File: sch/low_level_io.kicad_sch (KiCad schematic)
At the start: 10 parts, among them J401 Extension, SW401 RESET_Sw, SW402 USER_Sw

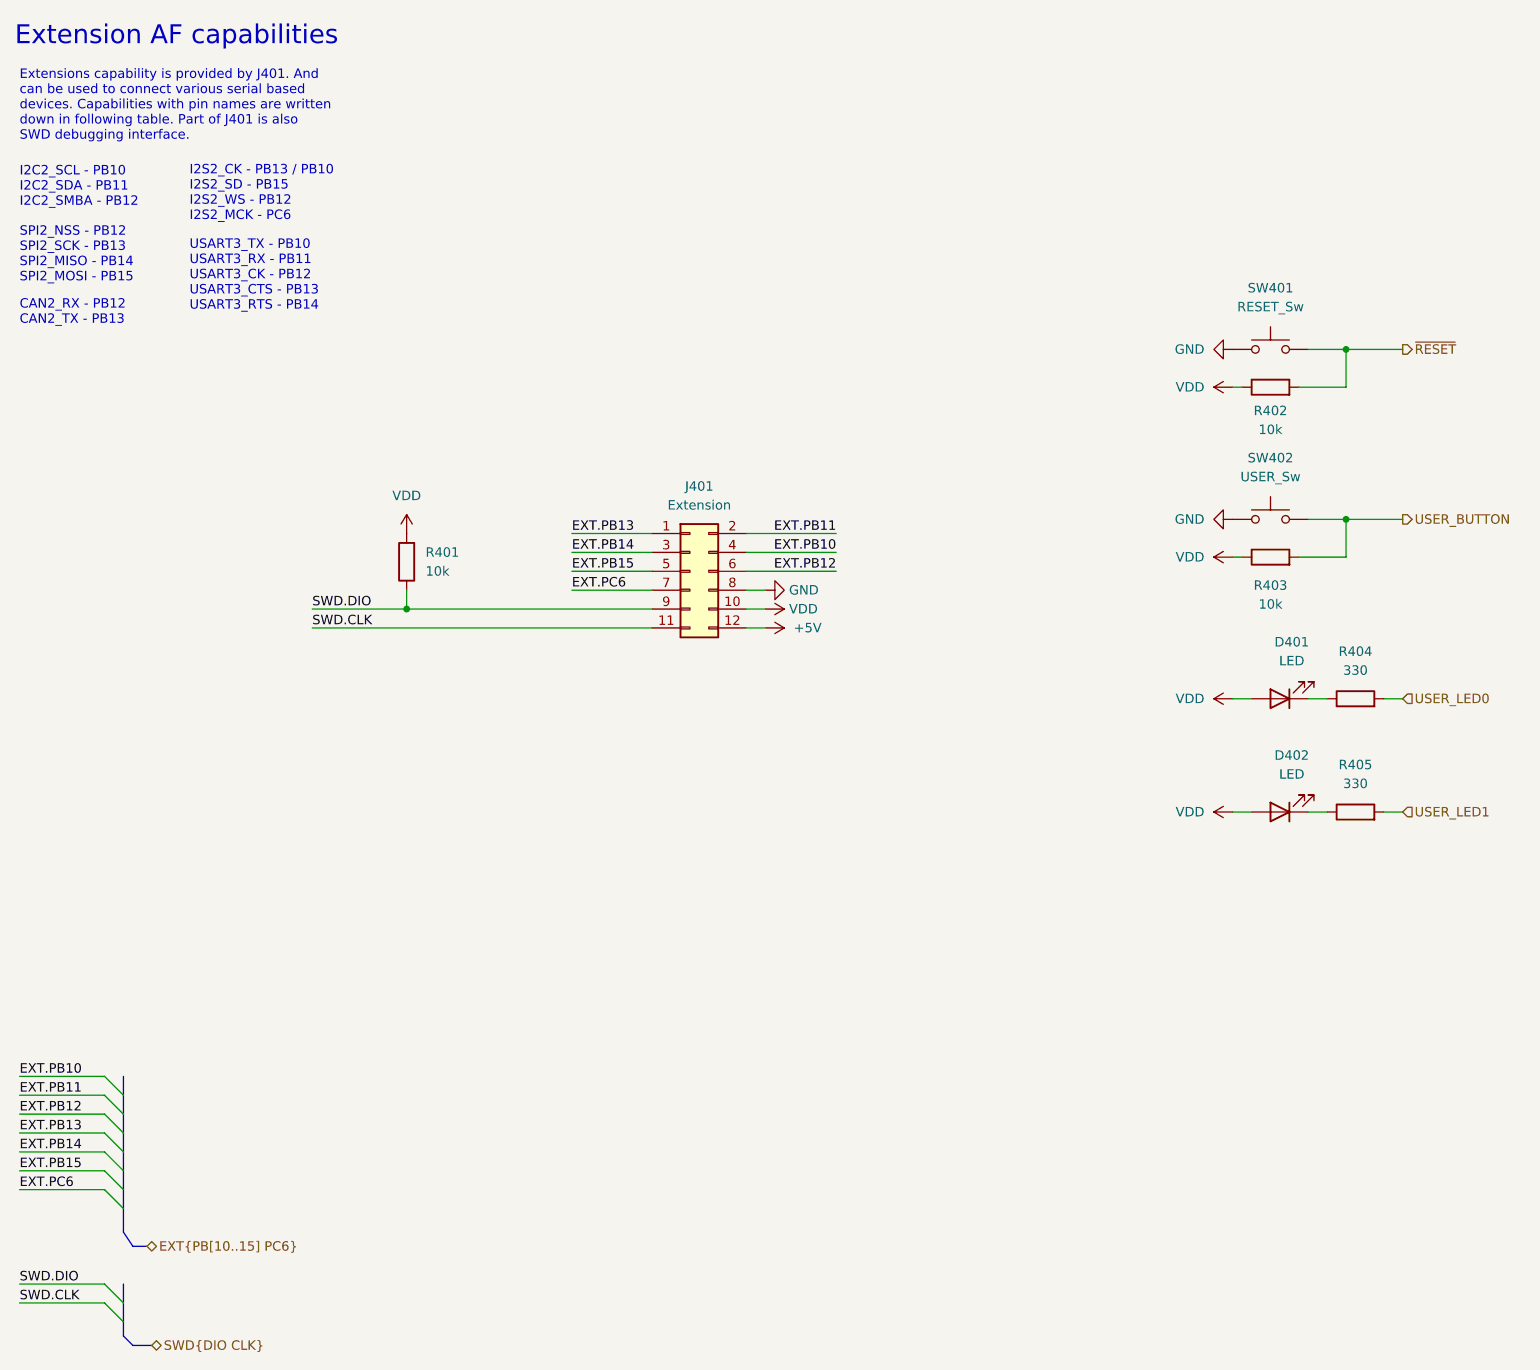
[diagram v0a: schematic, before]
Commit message: Added more expansion capability.
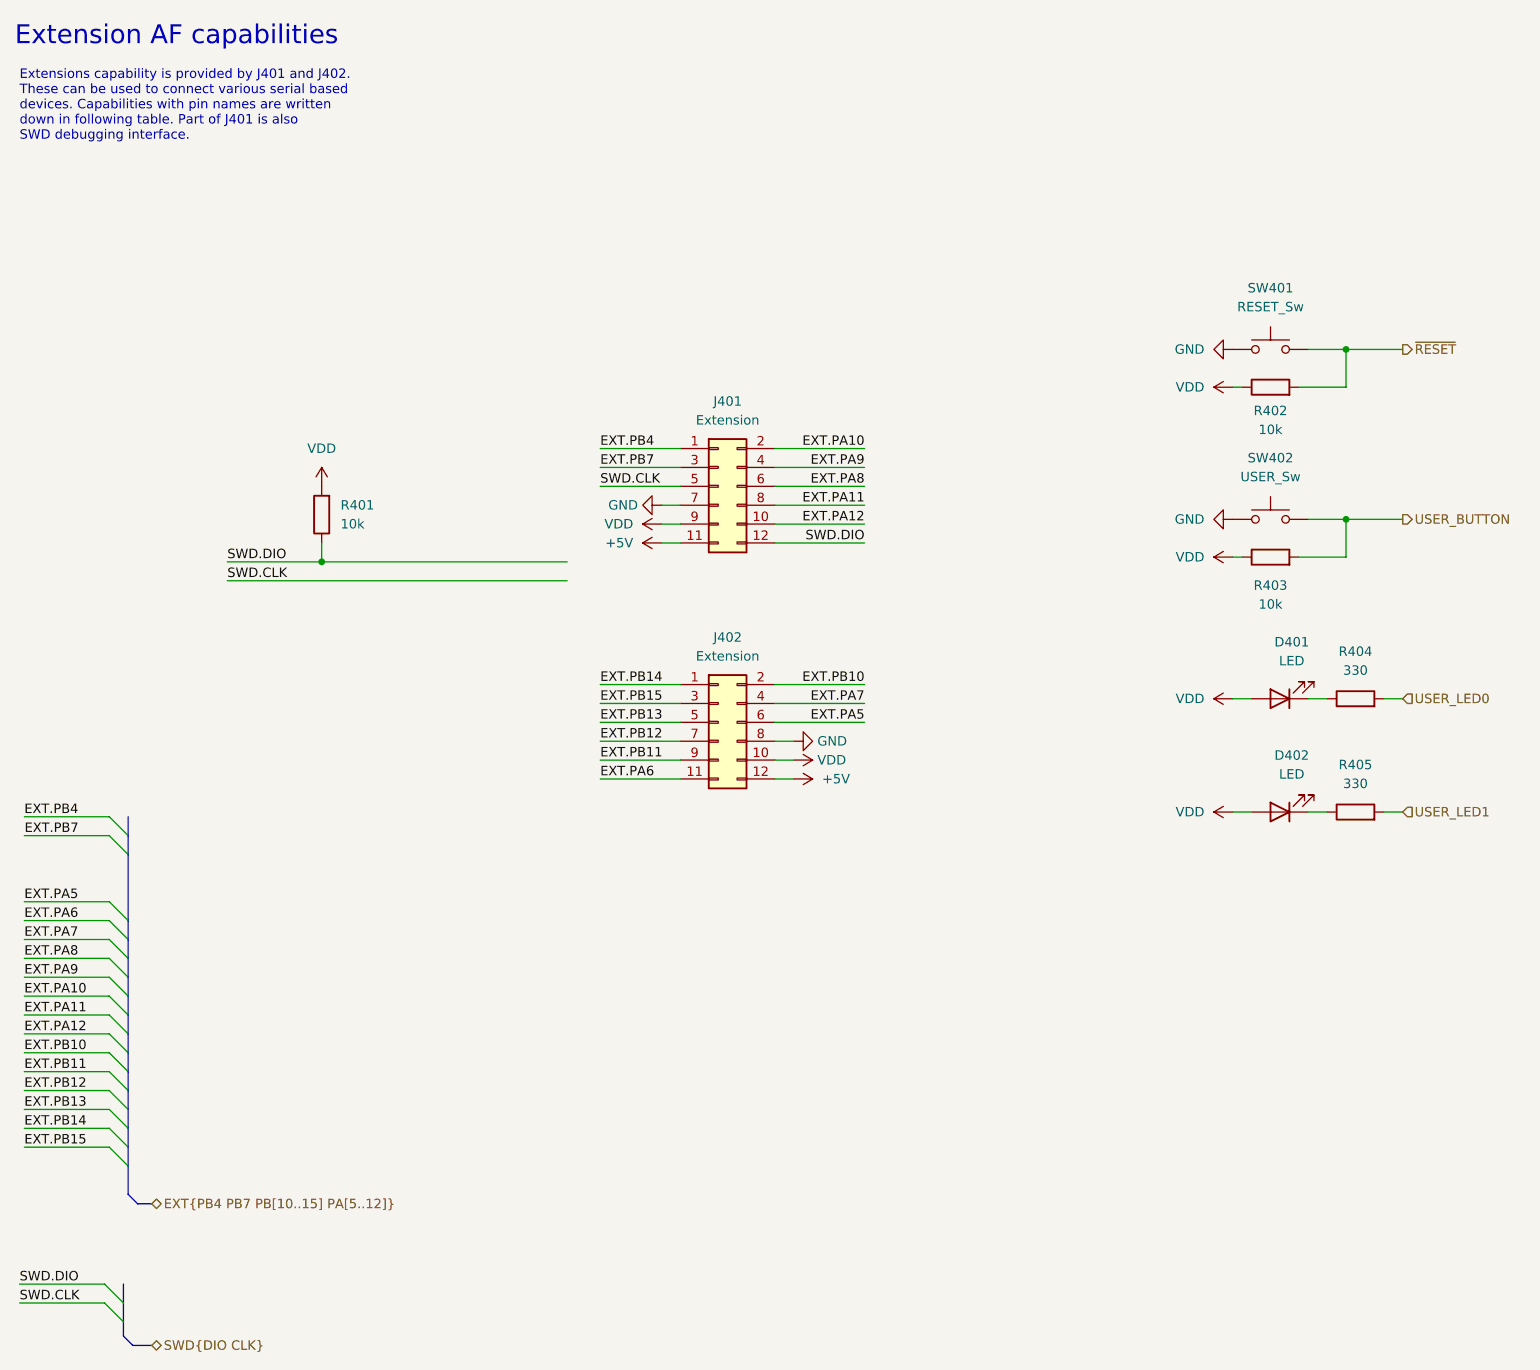
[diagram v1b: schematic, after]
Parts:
- added J402: Extension, Connector_PinSocket_2.54mm:PinSocket_2x06_P2.54mm_Vertical_SMD, symbol Connector_Generic:Conn_02x06_Odd_Even
- J401: footprint Connector_PinSocket_2.54mm:PinSocket_2x06_P2.54mm_Vertical -> Connector_PinSocket_2.54mm:PinSocket_2x06_P2.54mm_Vertical_SMD
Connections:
- net EXT.PC6 is gone; now on net GND: J401.7 (Pin_7)
- net +5V: now also J401.11 (Pin_11), J402.12 (Pin_12); no longer J401.12 (Pin_12)
- net EXT.PB10: now also J402.2 (Pin_2); no longer J401.4 (Pin_4)
- net EXT.PB11: now also J402.9 (Pin_9); no longer J401.2 (Pin_2)
- net EXT.PB12: now also J402.7 (Pin_7); no longer J401.6 (Pin_6)
- net EXT.PB13: now also J402.5 (Pin_5); no longer J401.1 (Pin_1)
- net EXT.PB14: now also J402.1 (Pin_1); no longer J401.3 (Pin_3)
- net EXT.PB15: now also J402.3 (Pin_3); no longer J401.5 (Pin_5)
- net GND: now also J402.8 (Pin_8); no longer J401.8 (Pin_8)
- net SWD.CLK: now also J401.5 (Pin_5); no longer J401.11 (Pin_11)
- net SWD.DIO: now also J401.12 (Pin_12); no longer J401.9 (Pin_9)
- net VDD: now also J401.9 (Pin_9), J402.10 (Pin_10); no longer J401.10 (Pin_10)
- new net EXT.PA10: J401.2 (Pin_2)
- new net EXT.PA11: J401.8 (Pin_8)
- new net EXT.PA12: J401.10 (Pin_10)
- new net EXT.PA5: J402.6 (Pin_6)
- new net EXT.PA6: J402.11 (Pin_11)
- new net EXT.PA7: J402.4 (Pin_4)
- new net EXT.PA8: J401.6 (Pin_6)
- new net EXT.PA9: J401.4 (Pin_4)
- new net EXT.PB4: J401.1 (Pin_1)
- new net EXT.PB7: J401.3 (Pin_3)
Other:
- note added: "Extensions capability is provided by J401 and J402. These can be used to connect various serial based devices. Capabilities with pin names are written down in following table. Part of J401 is also SWD debugging interface."
- note removed: "CAN2_RX - PB12 CAN2_TX - PB13"
- note removed: "Extensions capability is provided by J401. And can be used to connect various serial based devices. Capabilities with pin names are written down in following table. Part of J401 is also SWD debugging interface."
- note removed: "I2C2_SCL - PB10 I2C2_SDA - PB11 I2C2_SMBA - PB12"
- note removed: "I2S2_CK - PB13 / PB10 I2S2_SD - PB15 I2S2_WS - PB12 I2S2_MCK - PC6"
- note removed: "SPI2_NSS - PB12 SPI2_SCK - PB13 SPI2_MISO - PB14 SPI2_MOSI - PB15"
- note removed: "USART3_TX - PB10 USART3_RX - PB11 USART3_CK - PB12 USART3_CTS - PB13 USART3_RTS - PB14"
- moved on the sheet: J401, R401
